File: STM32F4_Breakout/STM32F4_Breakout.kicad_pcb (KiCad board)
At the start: 2 copper layers, 50 x 49.8 mm, 44 parts, among them J1 Conn_01x02, J2 Conn_01x02, J3 Conn_01x02, J4 Conn_02x05_Odd_Even, J5 Conn_01x04, J6 Conn_01x02, U1 AMS1117-3.3, U2 STM32F405RGT6

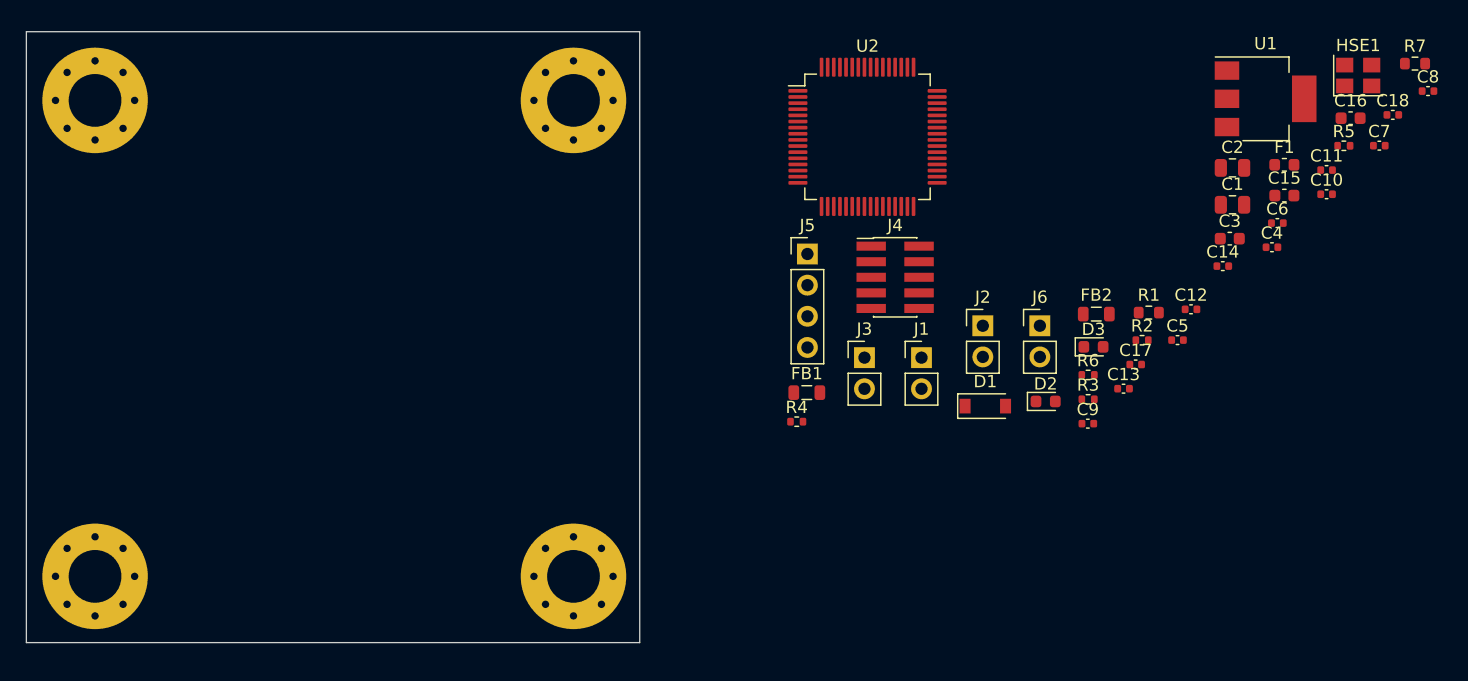
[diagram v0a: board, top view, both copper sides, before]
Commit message: resizing and shaping board
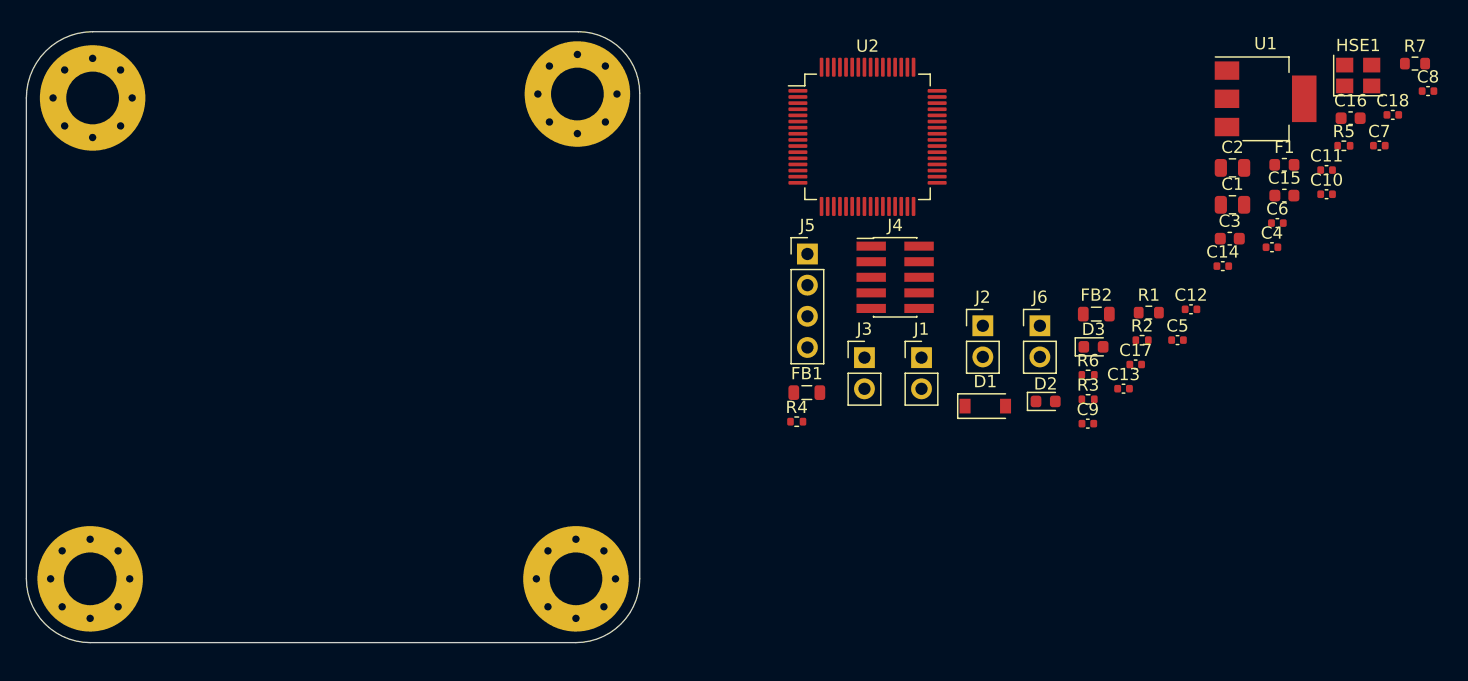
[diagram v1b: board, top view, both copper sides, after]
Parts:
- moved H3 0.61 mm to (105.3, 44.9)
- moved H1 0.45 mm to (65.6, 84.4)
- moved H2 0.28 mm to (105.2, 84.4)
- moved H4 0.28 mm to (65.8, 45.2)
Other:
- outline, holes or cut-outs redrawn
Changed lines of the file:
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@@
   )
   (footprint "MountingHole:MountingHole_4.3mm_M4_Pad_Via" (layer "F.Cu")
-    (at 105 84.2)
+    (at 105.2 84.4)
     (descr "Mounting Hole 4.3mm, M4")
     (tags "mounting hole 4.3mm m4")
@@
   )
   (footprint "MountingHole:MountingHole_4.3mm_M4_Pad_Via" (layer "F.Cu")
-    (at 105 45.4)
+    (at 105.319581 44.880419)
     (descr "Mounting Hole 4.3mm, M4")
     (tags "mounting hole 4.3mm m4")
@@
   )
   (footprint "MountingHole:MountingHole_4.3mm_M4_Pad_Via" (layer "F.Cu")
-    (at 66 45.4)
+    (at 65.8 45.2)
     (descr "Mounting Hole 4.3mm, M4")
     (tags "mounting hole 4.3mm m4")
@@
   )
   (footprint "MountingHole:MountingHole_4.3mm_M4_Pad_Via" (layer "F.Cu")
-    (at 66 84.2)
+    (at 65.6 84.4)
     (descr "Mounting Hole 4.3mm, M4")
     (tags "mounting hole 4.3mm m4")
@@
     )
   )
-  (gr_line (start 110.4 39.8) (end 110.4 89.6) (layer "Edge.Cuts") (width 0.1))
-  (gr_line (start 60.4 89.6) (end 60.4 39.8) (layer "Edge.Cuts") (width 0.1))
-  (gr_line (start 60.4 39.8) (end 110.4 39.8) (layer "Edge.Cuts") (width 0.1))
-  (gr_line (start 110.4 89.6) (end 60.4 89.6) (layer "Edge.Cuts") (width 0.1))
+  (gr_line (start 110.4 44.8) (end 110.4 84.4) (layer "Edge.Cuts") (width 0.1))
+  (gr_line (start 60.4 84.4) (end 60.4 45.2) (layer "Edge.Cuts") (width 0.1))
+  (gr_line (start 65.8 39.8) (end 105.4 39.8) (layer "Edge.Cuts") (width 0.1))
+  (gr_arc (start 65.6 89.6) (mid 61.923045 88.076955) (end 60.4 84.4) (layer "Edge.Cuts") (width 0.1))
+  (gr_line (start 105.2 89.6) (end 65.6 89.6) (layer "Edge.Cuts") (width 0.1))
+  (gr_arc (start 105.4 39.8) (mid 108.935534 41.264466) (end 110.4 44.8) (layer "Edge.Cuts") (width 0.1))
+  (gr_arc (start 110.4 84.4) (mid 108.876955 88.076955) (end 105.2 89.6) (layer "Edge.Cuts") (width 0.1))
+  (gr_arc (start 60.4 45.2) (mid 61.981623 41.381623) (end 65.8 39.8) (layer "Edge.Cuts") (width 0.1))
 )

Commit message: rough placement of filtering caps, ucontroller and oscillator circuit
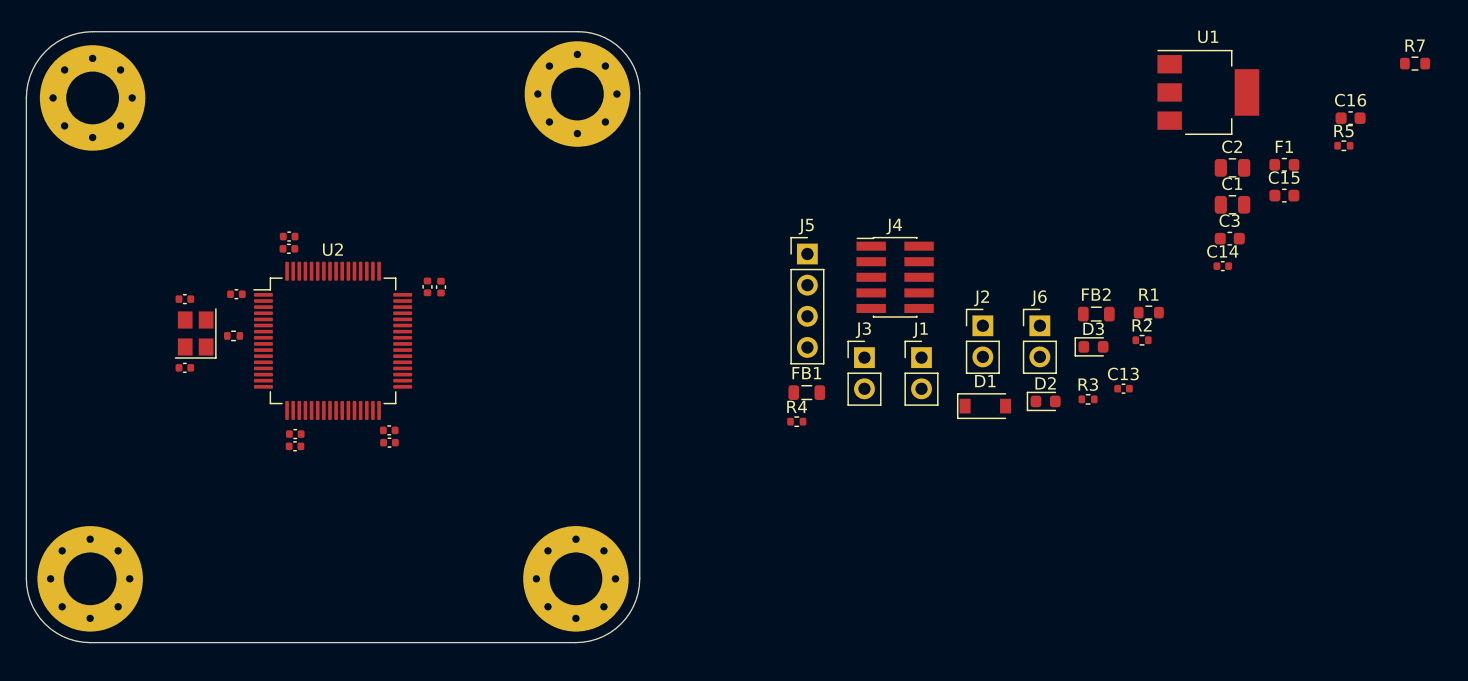
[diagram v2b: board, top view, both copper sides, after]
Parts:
- moved C18 100.6 mm to (73.3, 67.2)
- moved HSE1 97.1 mm to (74.2, 64.4), turned to 90 degrees
- moved C8 89.4 mm to (90.0, 73.3), turned to 180 degrees
- moved C11 84.8 mm to (81.8, 57.5)
- moved C4 84.5 mm to (77.5, 61.2), turned to 180 degrees
- moved C7 84.0 mm to (90.0, 72.3), turned to 180 degrees
- moved C6 82.1 mm to (82.3, 73.6), turned to 180 degrees
- moved C17 77.7 mm to (73.3, 61.6), turned to 180 degrees
- moved C12 73.8 mm to (81.8, 56.5)
- moved C10 72.6 mm to (94.2, 60.6), turned to 90 degrees
- moved C5 72.3 mm to (82.3, 72.6), turned to 180 degrees
- moved R6 69.7 mm to (77.3, 64.6), turned to 180 degrees
- moved C9 55.0 mm to (93.1, 60.6), turned to 90 degrees
- moved U2 46.6 mm to (85.4, 65.0)
- moved U1 4.70 mm to (156.8, 44.8)

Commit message: finishing ucontroller layout
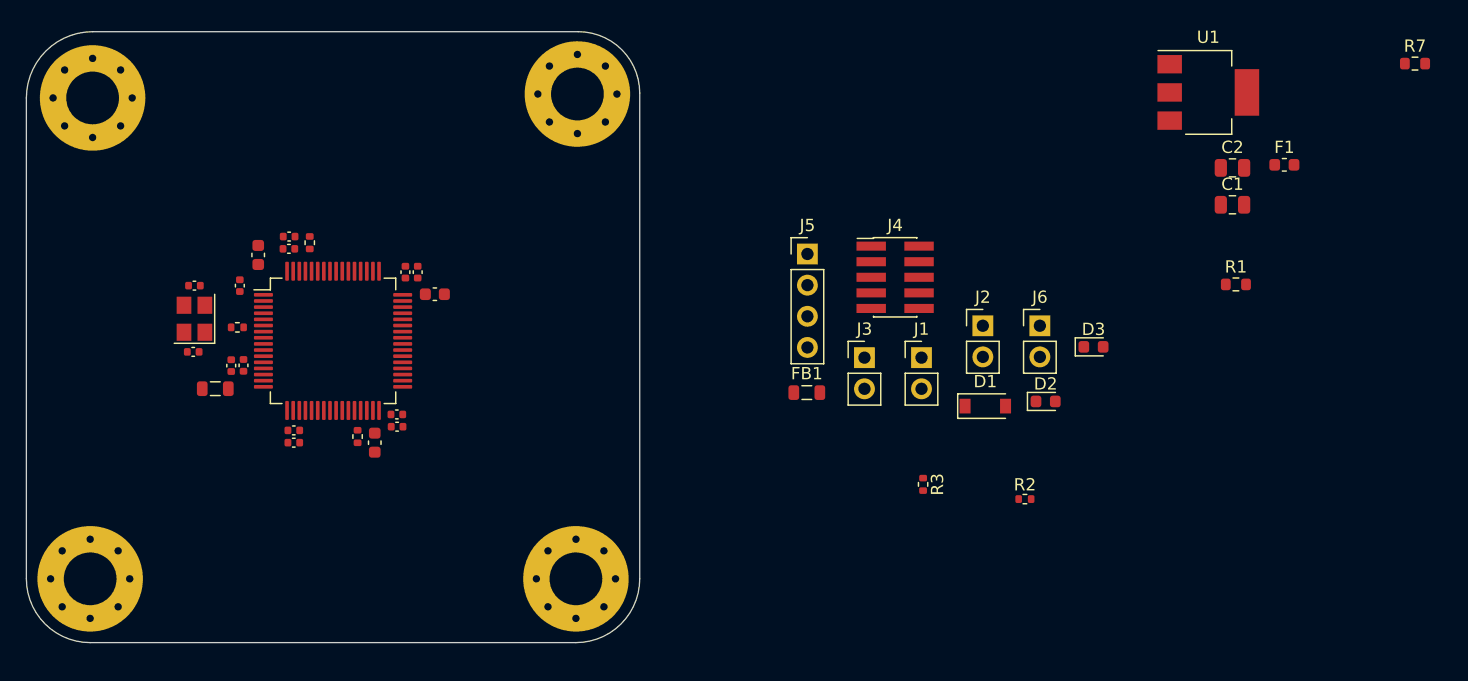
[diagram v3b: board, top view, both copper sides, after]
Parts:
- moved R5 83.8 mm to (87.4, 72.8), turned to 90 degrees
- moved C14 80.2 mm to (78.1, 67.0), turned to 90 degrees
- moved C3 79.2 mm to (79.3, 58.0), turned to 90 degrees
- moved C15 76.8 mm to (88.8, 73.3), turned to -90 degrees
- moved C16 76.0 mm to (93.7, 61.2)
- moved C13 72.8 mm to (77.1, 67.0), turned to 90 degrees
- moved FB2 72.1 mm to (75.8, 68.9), turned to 180 degrees
- moved R4 42.3 mm to (83.5, 57.0), turned to -90 degrees
- moved R2 16.1 mm to (141.8, 77.9)
- moved R3 15.1 mm to (133.5, 76.7), turned to -90 degrees
- moved R1 7.46 mm to (159.0, 60.4)
- moved C10 2.26 mm to (92.3, 59.4)
- moved C9 2.16 mm to (91.3, 59.4)
- moved C18 1.47 mm to (74.0, 65.9)
- moved C8 1.44 mm to (90.6, 72.0)
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
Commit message: laying out power supply and connectors
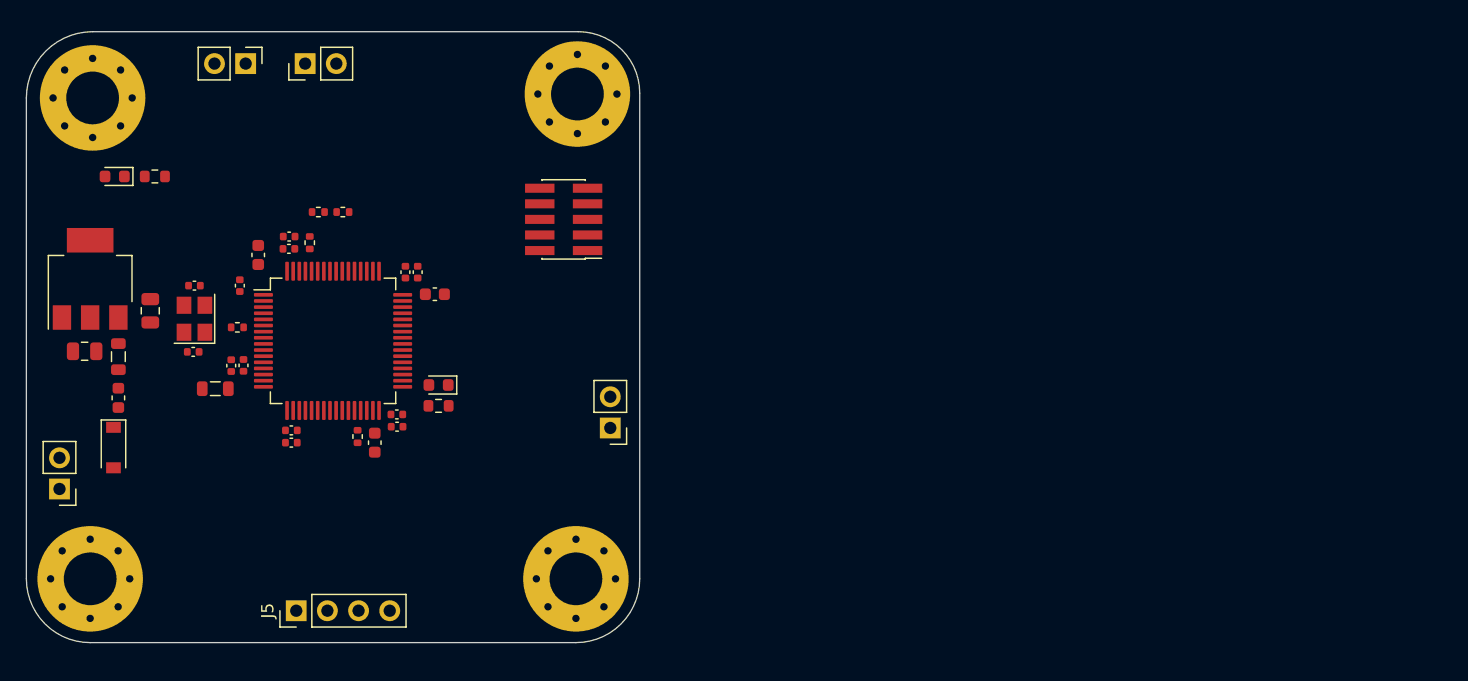
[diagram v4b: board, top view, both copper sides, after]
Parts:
- moved F1 96.9 mm to (67.9, 69.7), turned to 90 degrees
- moved C2 94.8 mm to (65.2, 65.8), turned to 180 degrees
- moved U1 92.4 mm to (65.6, 60.0), turned to 90 degrees
- moved C1 88.6 mm to (70.5, 62.5), turned to -90 degrees
- moved R1 88.6 mm to (70.9, 51.6), turned to 180 degrees
- moved R7 84.3 mm to (94.0, 70.3)
- moved D2 78.1 mm to (67.6, 51.6), turned to 180 degrees
- moved D1 71.2 mm to (67.5, 73.7), turned to -90 degrees
- moved J1 71.1 mm to (63.1, 77.1), turned to 180 degrees
- moved R2 62.2 mm to (84.2, 54.5), turned to 180 degrees
- moved J2 59.2 mm to (83.1, 42.4), turned to 90 degrees
- moved FB1 56.2 mm to (67.9, 66.3), turned to -90 degrees
- moved J3 55.9 mm to (78.3, 42.4), turned to -90 degrees
- moved D3 53.5 mm to (94.0, 68.6), turned to 180 degrees
- moved R3 52.3 mm to (86.2, 54.5), turned to 180 degrees
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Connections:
- J2 pad 1: I2C1_SCL -> I2C1_SDA
- J2 pad 2: I2C1_SDA -> I2C1_SCL

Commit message: setting up layers and design rules per jlcpcb
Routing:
- added copper zone on F.Cu, net GND
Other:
- copper layers 2 -> 4
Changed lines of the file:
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@@
 (kicad_pcb (version 20211014) (generator pcbnew)
   (general
-    (thickness 1.6)
+    (thickness 4.69)
   )
   (paper "A4")
   (layers
     (0 "F.Cu" signal)
+    (1 "In1.Cu" power)
+    (2 "In2.Cu" power)
     (31 "B.Cu" signal)
     (32 "B.Adhes" user "B.Adhesive")
@@
   )
   (setup
+    (stackup
+      (layer "F.SilkS" (type "Top Silk Screen"))
+      (layer "F.Paste" (type "Top Solder Paste"))
+      (layer "F.Mask" (type "Top Solder Mask") (thickness 0.01))
+      (layer "F.Cu" (type "copper") (thickness 0.035))
+      (layer "dielectric 1" (type "core") (thickness 1.51) (material "FR4") (epsilon_r 4.5) (loss_tangent 0.02))
+      (layer "In1.Cu" (type "copper") (thickness 0.035))
+      (layer "dielectric 2" (type "prepreg") (thickness 1.51) (material "FR4") (epsilon_r 4.5) (loss_tangent 0.02))
+      (layer "In2.Cu" (type "copper") (thickness 0.035))
+      (layer "dielectric 3" (type "core") (thickness 1.51) (material "FR4") (epsilon_r 4.5) (loss_tangent 0.02))
+      (layer "B.Cu" (type "copper") (thickness 0.035))
+      (layer "B.Mask" (type "Bottom Solder Mask") (thickness 0.01))
+      (layer "B.Paste" (type "Bottom Solder Paste"))
+      (layer "B.SilkS" (type "Bottom Silk Screen"))
+      (copper_finish "None")
+      (dielectric_constraints no)
+    )
     (pad_to_mask_clearance 0)
     (pcbplotparams
@@
   (gr_arc (start 110.4 84.4) (mid 108.876955 88.076955) (end 105.2 89.6) (layer "Edge.Cuts") (width 0.1))
   (gr_arc (start 60.4 45.2) (mid 61.981623 41.381623) (end 65.8 39.8) (layer "Edge.Cuts") (width 0.1))
+  (zone (net 1) (net_name "GND") (layer "F.Cu") (hatch edge 0.508)
+    (connect_pads (clearance 0.508))
+    (min_thickness 0.254) (filled_areas_thickness no)
+    (fill yes (thermal_gap 0.508) (thermal_bridge_width 0.508))
+    (polygon
+      (pts
+        (xy 81 61.5)
+        (xy 76.75 61.5)
+        (xy 76.75 59.5)
+        (xy 81 59.5)
+      )
+    )
+  )
+  (zone (net 1) (net_name "GND") (layer "F.Cu") (hatch edge 0.508)
+    (connect_pads (clearance 0.508))
+    (min_thickness 0.254) (filled_areas_thickness no)
+    (fill yes (thermal_gap 0.508) (thermal_bridge_width 0.508))
+    (polygon
+      (pts
+        (xy 71.75 65.75)
+        (xy 60.25 65.75)
+        (xy 60.25 59.5)
+        (xy 71.75 59.5)
+      )
+    )
+  )
+  (zone (net 1) (net_name "GND") (layer "F.Cu") (hatch edge 0.508)
+    (connect_pads (clearance 0.508))
+    (min_thickness 0.254) (filled_areas_thickness no)
+    (fill yes (thermal_gap 0.508) (thermal_bridge_width 0.508))
+    (polygon
+      (pts
+        (xy 110.5 90)
+        (xy 60.25 90)
+        (xy 60.25 65.75)
+        (xy 76.25 65.75)
+        (xy 76.25 64.75)
+        (xy 81 64.75)
+        (xy 81 59.5)
+        (xy 60.25 59.5)
+        (xy 60.25 39.75)
+        (xy 110.5 39.75)
+      )
+    )
+  )
 )
